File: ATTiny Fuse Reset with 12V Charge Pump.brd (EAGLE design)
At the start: 34 parts, among them U2 ARDUINOR3-BPLACE

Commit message: Changes in the schematic
MOSI, MISO, SCK and 12V_OFF are now connected to the correct pins of the
Arduino UNO
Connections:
- removed net SDI: JP11.4, JP12.1, R1.1, U2.D9
- removed net SDO: JP11.3, JP12.7, R3.1, U2.D11
- removed net SII: JP11.1, JP12.9, R2.1, U2.D10
- new net SDI-MOSI: JP11.4, JP12.1, R1.1, U2.D11
- new net SDO-SCK: JP11.3, JP12.7, R3.1, U2.D13
- new net SII-MISO: JP11.1, JP12.9, R2.1, U2.D12
- net 12V_OFF: now also U2.D10; no longer U2.D5
- net ATTINY_VCC: no longer U2.D8
- net N$9: now also U2.D8; no longer U2.D6
- net SCI: now also U2.D9; no longer U2.D12
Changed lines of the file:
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@@
 </signal>
 <signal name="ATTINY_VCC">
-<contactref element="U2" pad="D8"/>
 <contactref element="R10" pad="1"/>
 <contactref element="IC1" pad="8"/>
@@
 <contactref element="IC2" pad="8"/>
 <contactref element="LED1" pad="A"/>
-<wire x1="29.43" y1="27.94" x2="41.656" y2="50.8" width="0" layer="19" extent="1-1"/>
 <wire x1="28.84" y1="25.4" x2="29.43" y2="27.94" width="0" layer="19" extent="1-1"/>
 <wire x1="17.78" y1="33.02" x2="29.43" y2="27.94" width="0" layer="19" extent="1-1"/>
@@
 <contactref element="D5" pad="CQ"/>
 <contactref element="IC1" pad="1"/>
+<contactref element="JP12" pad="5"/>
 <contactref element="JP11" pad="5"/>
-<contactref element="JP12" pad="5"/>
 <wire x1="46.04" y1="43.01" x2="45.72" y2="46.09" width="0" layer="19" extent="1-1"/>
-<wire x1="25.4" y1="33.02" x2="45.72" y2="46.09" width="0" layer="19" extent="1-1"/>
+<wire x1="25.4" y1="33.02" x2="46.04" y2="43.01" width="0" layer="19" extent="1-1"/>
 <wire x1="25.4" y1="30.099" x2="25.4" y2="33.02" width="0" layer="19" extent="1-1"/>
 <wire x1="3.81" y1="33.02" x2="25.4" y2="33.02" width="0" layer="19" extent="1-1"/>
@@
 <wire x1="47.94" y1="43.01" x2="48.26" y2="46.09" width="0" layer="19" extent="1-1"/>
 </signal>
-<signal name="SDI">
+<signal name="SDI-MOSI">
 <contactref element="R1" pad="1"/>
-<contactref element="U2" pad="D9"/>
+<contactref element="JP11" pad="4"/>
+<contactref element="U2" pad="D11"/>
 <contactref element="JP12" pad="1"/>
-<contactref element="JP11" pad="4"/>
-<wire x1="39.37" y1="47.89" x2="39.116" y2="50.8" width="0" layer="19" extent="1-1"/>
+<wire x1="34.036" y1="50.8" x2="39.37" y2="47.89" width="0" layer="19" extent="1-1"/>
 <wire x1="50.8" y1="11.43" x2="39.37" y2="47.89" width="0" layer="19" extent="1-1"/>
 <wire x1="60.96" y1="8.89" x2="50.8" y2="11.43" width="0" layer="19" extent="1-1"/>
 </signal>
-<signal name="SII">
+<signal name="SII-MISO">
 <contactref element="R2" pad="1"/>
-<contactref element="U2" pad="D10"/>
 <contactref element="JP12" pad="9"/>
 <contactref element="JP11" pad="1"/>
-<wire x1="36.83" y1="47.89" x2="36.576" y2="50.8" width="0" layer="19" extent="1-1"/>
+<contactref element="U2" pad="D12"/>
+<wire x1="31.496" y1="50.8" x2="36.83" y2="47.89" width="0" layer="19" extent="1-1"/>
 <wire x1="40.64" y1="11.43" x2="36.83" y2="47.89" width="0" layer="19" extent="1-1"/>
 <wire x1="63.5" y1="11.43" x2="40.64" y2="11.43" width="0" layer="19" extent="1-1"/>
 </signal>
-<signal name="SDO">
+<signal name="SDO-SCK">
 <contactref element="R3" pad="1"/>
-<contactref element="U2" pad="D11"/>
 <contactref element="JP12" pad="7"/>
 <contactref element="JP11" pad="3"/>
-<wire x1="33.655" y1="47.89" x2="34.036" y2="50.8" width="0" layer="19" extent="1-1"/>
+<contactref element="U2" pad="D13"/>
+<wire x1="28.956" y1="50.8" x2="33.655" y2="47.89" width="0" layer="19" extent="1-1"/>
 <wire x1="43.18" y1="11.43" x2="33.655" y2="47.89" width="0" layer="19" extent="1-1"/>
 <wire x1="60.96" y1="11.43" x2="43.18" y2="11.43" width="0" layer="19" extent="1-1"/>
@@
 <signal name="SCI">
 <contactref element="R4" pad="1"/>
-<contactref element="U2" pad="D12"/>
-<wire x1="31.75" y1="47.89" x2="31.496" y2="50.8" width="0" layer="19" extent="1-1"/>
+<contactref element="U2" pad="D9"/>
+<wire x1="31.75" y1="47.89" x2="39.116" y2="50.8" width="0" layer="19" extent="1-1"/>
 </signal>
 <signal name="12V_SENSE">
@@
 <wire x1="35.56" y1="38.47" x2="40.64" y2="38.47" width="0" layer="19" extent="1-1"/>
 <wire x1="50.8" y1="2.54" x2="40.64" y2="38.47" width="0" layer="19" extent="1-1"/>
-</signal>
-<signal name="12V_OFF">
-<contactref element="R5" pad="2"/>
-<contactref element="U2" pad="D5"/>
-<wire x1="48.26" y1="47.89" x2="50.8" y2="50.8" width="0" layer="19" extent="1-1"/>
 </signal>
 <signal name="N$8">
@@
 <signal name="N$9">
 <contactref element="U$7" pad="S"/>
-<contactref element="U2" pad="D6"/>
-<wire x1="65.06" y1="28.92" x2="48.26" y2="50.8" width="0" layer="19" extent="1-1"/>
+<contactref element="U2" pad="D8"/>
+<wire x1="41.656" y1="50.8" x2="65.06" y2="28.92" width="0" layer="19" extent="1-1"/>
 </signal>
 <signal name="N$7">
@@
 <wire x1="35.56" y1="40.27" x2="35.56" y2="42.28" width="0" layer="19" extent="1-1"/>
 </signal>
+<signal name="12V_OFF">
+<contactref element="R5" pad="2"/>
+<contactref element="U2" pad="D10"/>
+<wire x1="36.576" y1="50.8" x2="48.26" y2="47.89" width="0" layer="19" extent="1-1"/>
+</signal>
 </signals>

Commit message: error correction: ATTINY_VCC wire was not connected
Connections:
- net ATTINY_VCC: now also U2.D8
- net N$9: now also U2.D7; no longer U2.D8
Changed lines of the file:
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@@
 <contactref element="IC2" pad="8"/>
 <contactref element="LED1" pad="A"/>
+<contactref element="U2" pad="D8"/>
+<wire x1="29.43" y1="27.94" x2="41.656" y2="50.8" width="0" layer="19" extent="1-1"/>
 <wire x1="28.84" y1="25.4" x2="29.43" y2="27.94" width="0" layer="19" extent="1-1"/>
 <wire x1="17.78" y1="33.02" x2="29.43" y2="27.94" width="0" layer="19" extent="1-1"/>
@@
 <signal name="N$9">
 <contactref element="U$7" pad="S"/>
-<contactref element="U2" pad="D8"/>
-<wire x1="41.656" y1="50.8" x2="65.06" y2="28.92" width="0" layer="19" extent="1-1"/>
+<contactref element="U2" pad="D7"/>
+<wire x1="65.06" y1="28.92" x2="45.72" y2="50.8" width="0" layer="19" extent="1-1"/>
 </signal>
 <signal name="N$7">

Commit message: Some more corrections
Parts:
- added R11: 1K, ATtami:0805
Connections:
- removed net N$19: R5.1, T1.1
- new net N$1: R11.1, R5.1, T1.1
- net 12V_OFF: now also U2.D5; no longer U2.D10
- net GND: now also R11.2
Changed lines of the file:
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@@
 <element name="-HEADERS2" library="ATtami" package="BREAKOUT_ATTAMI_HEADERS-ONLY" value="" x="25.4" y="0" smashed="yes" rot="MR0"/>
 <element name="-HEADERS3" library="ATtami" package="BREAKOUT_ATTAMI" value="" x="58.42" y="15.24" rot="R90"/>
+<element name="R11" library="ATtami" package="0805" value="1K" x="2.54" y="-5.08"/>
 </elements>
 <signals>
@@
 <contactref element="IC2" pad="14"/>
 <contactref element="IC2" pad="11"/>
+<contactref element="R11" pad="2"/>
 <wire x1="62.595" y1="27.94" x2="65.06" y2="27.42" width="0" layer="19" extent="1-1"/>
 <wire x1="58.42" y1="8.89" x2="62.595" y2="27.94" width="0" layer="19" extent="1-1"/>
@@
 <wire x1="11.43" y1="35.56" x2="11.43" y2="38.1" width="0" layer="19" extent="1-1"/>
 <wire x1="11.43" y1="33.02" x2="11.43" y2="35.56" width="0" layer="19" extent="1-1"/>
+<wire x1="3.44" y1="-5.08" x2="40.64" y2="2.54" width="0" layer="19" extent="1-1"/>
 </signal>
 <signal name="VIN">
@@
 <wire x1="58.42" y1="11.43" x2="45.72" y2="11.43" width="0" layer="19" extent="1-1"/>
 </signal>
-<signal name="N$19">
-<contactref element="R5" pad="1"/>
-<contactref element="T1" pad="1"/>
-<wire x1="47.94" y1="43.01" x2="48.26" y2="46.09" width="0" layer="19" extent="1-1"/>
-</signal>
 <signal name="SDI-MOSI">
 <contactref element="R1" pad="1"/>
@@
 <signal name="12V_OFF">
 <contactref element="R5" pad="2"/>
-<contactref element="U2" pad="D10"/>
-<wire x1="36.576" y1="50.8" x2="48.26" y2="47.89" width="0" layer="19" extent="1-1"/>
+<contactref element="U2" pad="D5"/>
+<wire x1="48.26" y1="47.89" x2="50.8" y2="50.8" width="0" layer="19" extent="1-1"/>
+</signal>
+<signal name="N$1">
+<contactref element="R5" pad="1"/>
+<contactref element="T1" pad="1"/>
+<contactref element="R11" pad="1"/>
+<wire x1="47.94" y1="43.01" x2="48.26" y2="46.09" width="0" layer="19" extent="1-1"/>
+<wire x1="1.64" y1="-5.08" x2="47.94" y2="43.01" width="0" layer="19" extent="1-1"/>
 </signal>
 </signals>

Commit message: R6, R10 and R11 values changed
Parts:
- R10: value 10k -> 1k
- R11, R6: value 1K -> 10K
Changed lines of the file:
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@@
 <element name="R4" library="ATtami" package="0805" value="1K" x="31.75" y="46.99" rot="R270"/>
 <element name="R5" library="ATtami" package="0805" value="10K" x="48.26" y="46.99" rot="R90"/>
-<element name="R6" library="ATtami" package="0805" value="1K" x="45.72" y="46.99" rot="R90"/>
+<element name="R6" library="ATtami" package="0805" value="10K" x="45.72" y="46.99" rot="R90"/>
 <element name="R7" library="ATtami" package="0805" value="510K" x="35.56" y="39.37" rot="R90"/>
 <element name="R8" library="ATtami" package="0805" value="100K" x="40.64" y="39.37" rot="R270"/>
@@
 <element name="R9" library="ATtami" package="0805" value="1K" x="43.18" y="39.37" rot="R90"/>
 <element name="LED1" library="ATtami" package="LED-805" value="" x="30.48" y="27.94" rot="R270"/>
-<element name="R10" library="ATtami" package="0805" value="10k" x="27.94" y="25.4" rot="R180"/>
+<element name="R10" library="ATtami" package="0805" value="1k" x="27.94" y="25.4" rot="R180"/>
 <element name="D5" library="ATtami" package="SOD-323" value="1N4148" x="25.4" y="27.94" rot="R270"/>
 <element name="JP11" library="SparkFun-Connectors" package="2X3-SHROUDED" value="" x="60.96" y="10.16" rot="R270">
@@
 <element name="-HEADERS2" library="ATtami" package="BREAKOUT_ATTAMI_HEADERS-ONLY" value="" x="25.4" y="0" smashed="yes" rot="MR0"/>
 <element name="-HEADERS3" library="ATtami" package="BREAKOUT_ATTAMI" value="" x="58.42" y="15.24" rot="R90"/>
-<element name="R11" library="ATtami" package="0805" value="1K" x="2.54" y="-5.08"/>
+<element name="R11" library="ATtami" package="0805" value="10K" x="2.54" y="-5.08"/>
 </elements>
 <signals>

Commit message: Changes in the schematic
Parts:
- added C6: 2uF, ATtami:0805
- added R12: 10K, ATtami:0805
- -HEADERS1: value (none) -> ATTami
- IC1: value (none) -> ATTinyx5/13
- IC2: value (none) -> ATTinyx4
- JP11: value (none) -> 6 pin ISP
- JP12: value (none) -> 10 pin ISP
- R6: value 10K -> 2.2K
- R9: value 1K -> 220R
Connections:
- removed net N$13: IC1.6, R2.2
- removed net N$14: IC1.2, IC2.2, R4.2
- removed net SDI-MOSI: JP11.4, JP12.1, R1.1, U2.D11
- new net N$21: R1.1, U2.D11
- new net N$7: R3.1, U2.D13
- new net SDI_MOSI: IC1.5, IC2.7, JP11.4, JP12.1, R1.2
- net ATTINY_VCC: now also C6.1; no longer IC2.8
- net GND: now also C6.2
- net N$2: now also R4.1, U2.D9; no longer IC1.5, IC2.7, R1.2
- net N$8: now also R2.1, U2.D12; no longer IC1.7, IC2.9, R3.2
- net N$9: now also R12.2
- net SCI: now also IC1.2, IC2.2, R4.2; no longer R4.1, U2.D9
- net SDO-SCK: now also IC1.7, IC2.9, R3.2; no longer R3.1, U2.D13
- net SII-MISO: now also IC1.6, IC2.8, R2.2; no longer R2.1, U2.D12
- net VCC: now also R12.1

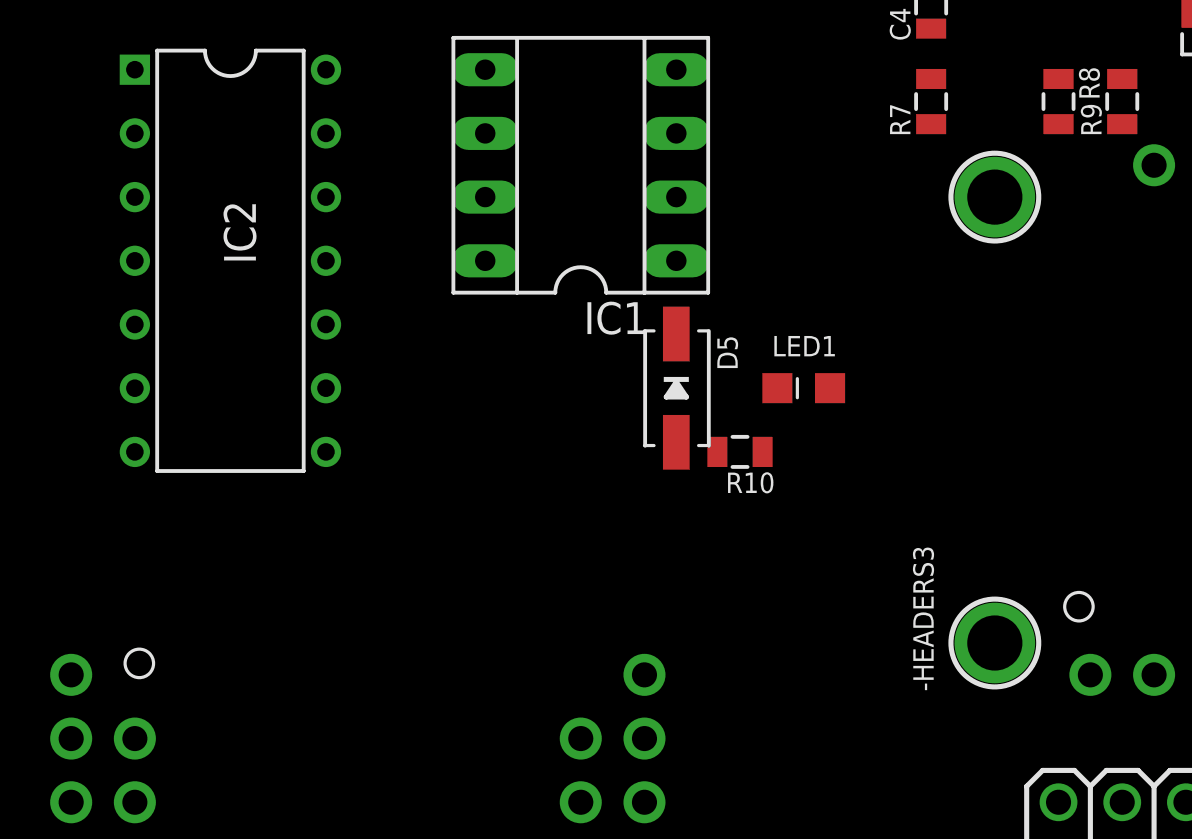
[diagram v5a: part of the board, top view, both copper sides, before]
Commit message: changed attiny breakout size
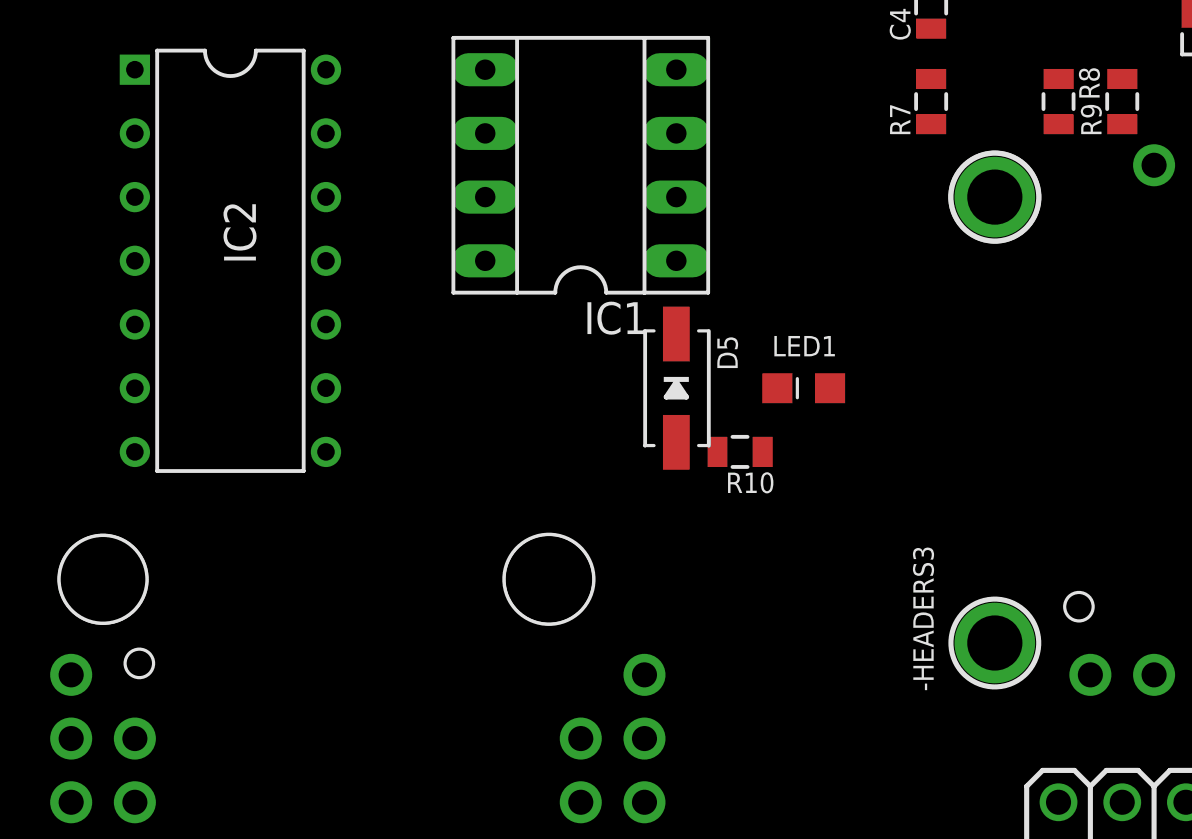
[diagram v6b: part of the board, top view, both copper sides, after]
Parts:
- -HEADERS1, -HEADERS2: device ATtami:BREAKOUT_ATTAMI_HEADERS-ONLY -> ATtami:BREAKOUT_ATTAMI
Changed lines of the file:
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@@
 <attribute name="NAME" x="59.69" y="29.21" size="1.27" layer="25" font="vector" ratio="10"/>
 </element>
-<element name="-HEADERS1" library="ATtami" package="BREAKOUT_ATTAMI_HEADERS-ONLY" value="ATTami" x="0" y="0" smashed="yes"/>
-<element name="-HEADERS2" library="ATtami" package="BREAKOUT_ATTAMI_HEADERS-ONLY" value="" x="25.4" y="0" smashed="yes" rot="MR0"/>
+<element name="-HEADERS1" library="ATtami" package="BREAKOUT_ATTAMI" value="ATTami" x="0" y="0" smashed="yes"/>
+<element name="-HEADERS2" library="ATtami" package="BREAKOUT_ATTAMI" value="" x="25.4" y="0" smashed="yes" rot="MR0"/>
 <element name="-HEADERS3" library="ATtami" package="BREAKOUT_ATTAMI" value="" x="58.42" y="15.24" rot="R90"/>
 <element name="R11" library="ATtami" package="0805" value="10K" x="2.54" y="-5.08"/>

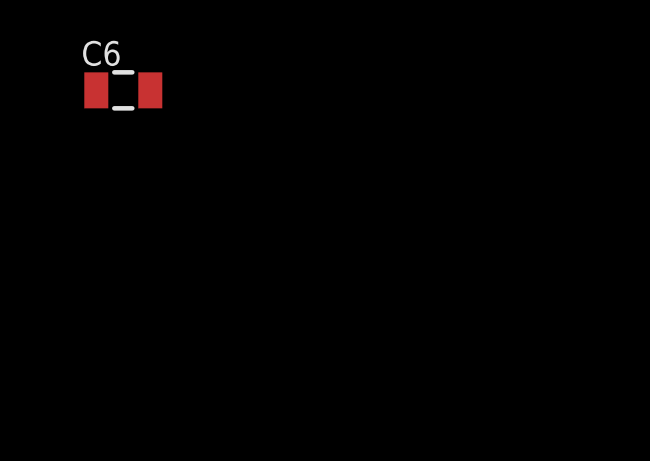
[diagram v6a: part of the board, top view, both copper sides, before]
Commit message: ATTami components connected
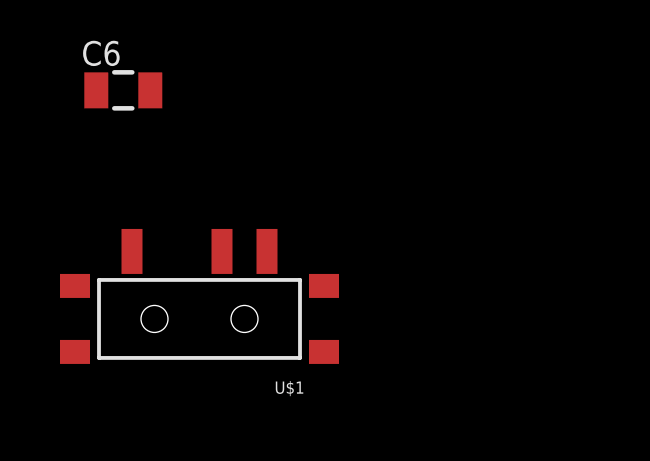
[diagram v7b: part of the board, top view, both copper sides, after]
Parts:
- added U$1: SWITCH_SPDT, SparkFun-Electromechanical:KPS-1290
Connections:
- new net ISP_VCC: JP11.2, JP12.2, U$1.S
- new net N$13: -HEADERS2.8
- net ATTINY_VCC: now also -HEADERS1.9, -HEADERS2.9, -HEADERS3.9
- net GND: now also -HEADERS1.10, -HEADERS1.8, -HEADERS2.10, -HEADERS3.10, -HEADERS3.8
- net HV/RESET: now also -HEADERS1.7, -HEADERS2.7, -HEADERS3.7
- net SCI: now also -HEADERS1.5, -HEADERS2.5, -HEADERS3.5
- net SDI_MOSI: now also -HEADERS1.2, -HEADERS2.2, -HEADERS3.2
- net SDO-SCK: now also -HEADERS1.4, -HEADERS2.4, -HEADERS3.4
- net SII-MISO: now also -HEADERS1.3, -HEADERS3.3
- net VCC: now also U$1.P; no longer JP11.2, JP12.2
